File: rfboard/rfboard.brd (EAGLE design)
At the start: 30 x 60 mm, 30 parts, among them Q1 IRLML5203, Q2 IRLML5203, Q3 IRLML5203, Q4 IRLML5203, Q5 IRLML5203

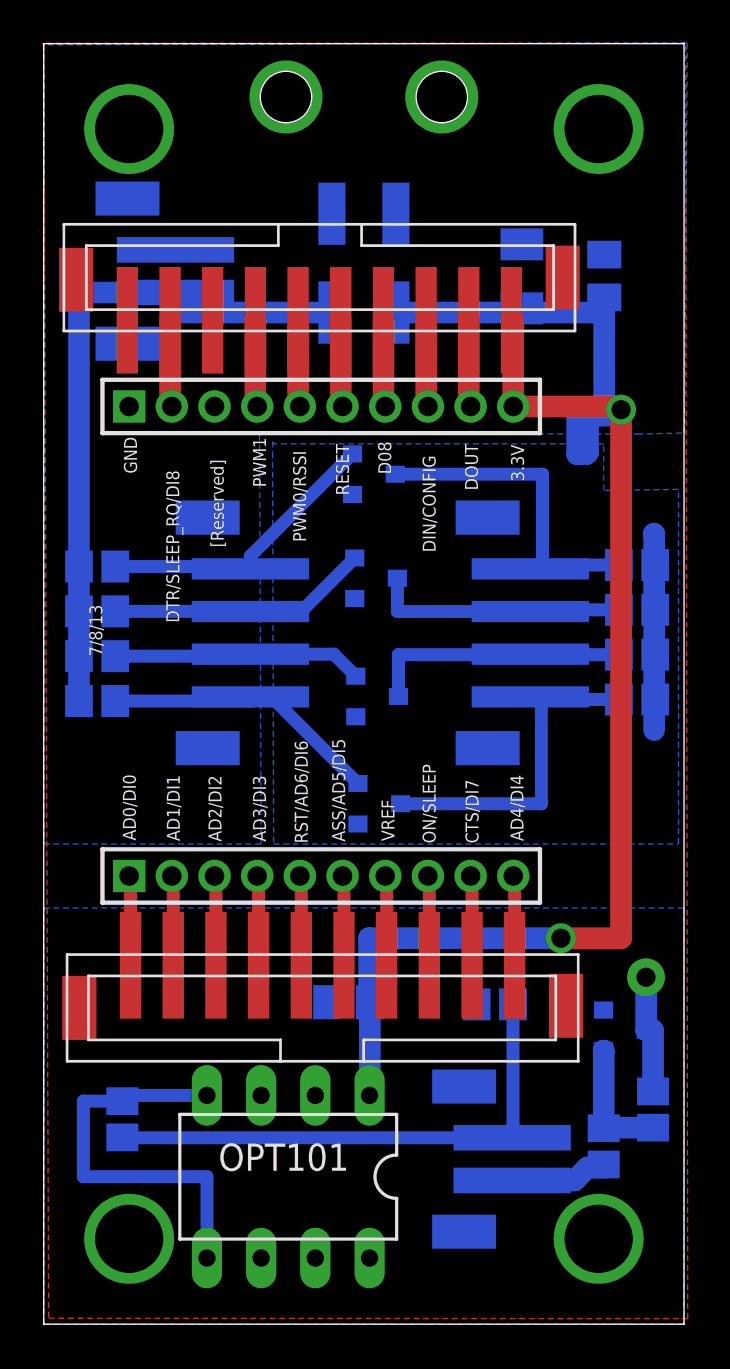
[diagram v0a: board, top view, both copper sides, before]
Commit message: resolved Sparkfun DRC errors, except for in-between pin errors
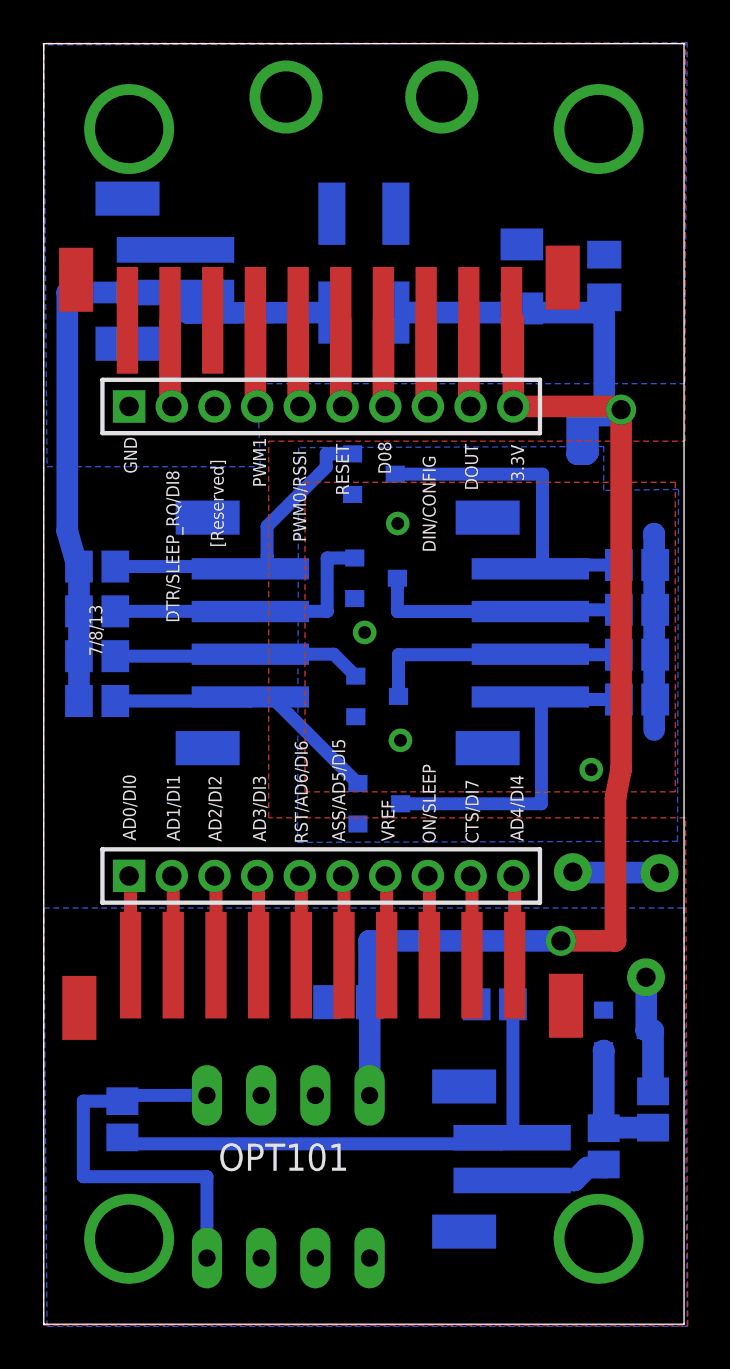
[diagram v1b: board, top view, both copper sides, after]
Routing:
- net GND: track 5.68 -> 9.69 mm, vias 1 -> 3
- net H2: track 12.3 -> 13.7 mm
- net H1: track 13.8 -> 15.0 mm
- net AMB_LOW: track 24.5 -> 25.1 mm
- net 3.3V: track 84.0 -> 83.8 mm, vias 2 -> 6
- added copper zone on layer 1, net 3.3V

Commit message: hole size, wire distance fixes, no soldermask changes yet
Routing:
- net GND: track 9.69 -> 72.3 mm, vias 3 -> 5
- net 3.3V: track 83.8 -> 84.6 mm
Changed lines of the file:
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@@
 <contactref element="C18" pad="2"/>
 <contactref element="C19" pad="2"/>
-<polygon width="0.508" layer="16" isolate="0.254">
+<polygon width="0.508" layer="16" isolate="0.3048">
 <vertex x="0.1524" y="40.1784"/>
-<vertex x="10.1524" y="40.1784"/>
-<vertex x="10" y="44.069"/>
-<vertex x="30.0228" y="44.069"/>
+<vertex x="5.2248" y="40.2038"/>
+<vertex x="5.1486" y="46.736"/>
+<vertex x="29.972" y="46.6852"/>
 <vertex x="30.1498" y="60.0456"/>
 <vertex x="0" y="59.944"/>
@@
 <via x="28.8544" y="21.1328" extent="1-16" drill="0.9" diameter="1.778"/>
 <via x="24.7904" y="21.1836" extent="1-16" drill="0.9" diameter="1.778"/>
-<wire x1="24.7904" y1="21.1582" x2="28.8036" y2="21.1582" width="1.016" layer="16"/>
-<wire x1="24.7904" y1="21.1836" x2="24.7904" y2="21.1582" width="0" layer="19" extent="16-16"/>
-<wire x1="28.8544" y1="21.1328" x2="28.8036" y2="21.1582" width="0" layer="19" extent="16-16"/>
-<wire x1="6.1724" y1="50.3394" x2="3.917" y2="47.0366" width="0" layer="19" extent="1-16"/>
+<wire x1="24.7904" y1="21.1582" x2="28.448" y2="21.1582" width="1.016" layer="16"/>
+<wire x1="28.448" y1="21.1582" x2="28.8036" y2="21.1582" width="1.016" layer="16"/>
+<wire x1="28.448" y1="21.336" x2="28.448" y2="21.1582" width="0.508" layer="16"/>
+<wire x1="28.448" y1="21.336" x2="28.8544" y2="21.1328" width="0.508" layer="16"/>
+<wire x1="22.86" y1="22.86" x2="24.384" y2="21.336" width="0.508" layer="16"/>
+<wire x1="16.256" y1="22.86" x2="22.86" y2="22.86" width="0.508" layer="16"/>
+<wire x1="3.048" y1="22.86" x2="16.256" y2="22.86" width="0.508" layer="1"/>
+<wire x1="3.048" y1="45.212" x2="3.048" y2="22.86" width="0.508" layer="1"/>
+<wire x1="4.572" y1="46.736" x2="3.048" y2="45.212" width="0.508" layer="1"/>
+<wire x1="4.572" y1="49.784" x2="4.572" y2="46.736" width="0.508" layer="1"/>
+<wire x1="9.144" y1="54.356" x2="4.572" y2="49.784" width="0.508" layer="1"/>
+<wire x1="14.732" y1="54.356" x2="9.144" y2="54.356" width="0.508" layer="1"/>
+<wire x1="24.384" y1="21.336" x2="24.7904" y2="21.1836" width="0.508" layer="16"/>
+<via x="16.256" y="22.86" extent="1-16" drill="0.508"/>
+<via x="14.732" y="54.356" extent="1-16" drill="0.508"/>
+<wire x1="24.7904" y1="21.1582" x2="24.7904" y2="21.1836" width="0" layer="19" extent="16-16"/>
 </signal>
 <signal name="AMB_OUT">
@@
 <contactref element="U$3" pad="P$1"/>
 <contactref element="X1" pad="P$3"/>
-<wire x1="16.5" y1="47.4" x2="26.2612" y2="47.4" width="1.016" layer="16"/>
+<wire x1="16.5" y1="47.4" x2="22.86" y2="47.4" width="1.016" layer="16"/>
+<wire x1="22.86" y1="47.4" x2="26.2612" y2="47.4" width="1.016" layer="16"/>
 <wire x1="26.2612" y1="47.4" x2="26.2612" y2="48.1146" width="1.016" layer="16"/>
 <via x="24.2316" y="17.9578" extent="1-16" drill="0.9"/>
@@
 <via x="16.5862" y="37.5158" extent="1-16" drill="0.6"/>
 <via x="15.0368" y="32.4104" extent="1-16" drill="0.6"/>
-<wire x1="22" y1="47.0366" x2="22.4036" y2="47.5946" width="0" layer="19" extent="1-16"/>
+<wire x1="22.86" y1="47.752" x2="22.4036" y2="47.5946" width="0.508" layer="16"/>
+<wire x1="22.86" y1="47.752" x2="22.86" y2="47.4" width="0.508" layer="16"/>
+<wire x1="14.7226" y1="23.434" x2="16.7132" y2="27.3558" width="0" layer="19" extent="16-16"/>
 </signal>
 <signal name="5V" class="1">
@@
 <signal name="DTR/SLEEP_RQ/D18">
 <contactref element="U$3" pad="P$9"/>
-<wire x1="5.917" y1="43" x2="5.917" y2="47.0366" width="1.016" layer="1"/>
+<wire x1="5.917" y1="43" x2="5.917" y2="43.18" width="1.016" layer="1"/>
 <contactref element="JP1" pad="2"/>
-<wire x1="6" y1="43" x2="5.917" y2="43" width="0" layer="19" extent="1-1"/>
+<wire x1="5.917" y1="43.18" x2="5.917" y2="47.0366" width="1.016" layer="1"/>
+<wire x1="6.096" y1="43.18" x2="6" y2="43" width="0.254" layer="1"/>
+<wire x1="6.096" y1="43.18" x2="5.917" y2="43.18" width="0.254" layer="1"/>
 </signal>
 <signal name="PWM1">
@@
 <contactref element="R8" pad="2"/>
 <wire x1="16.7226" y1="24.384" x2="23.3172" y2="24.384" width="0.6096" layer="16"/>
-<wire x1="23.3172" y1="24.384" x2="23.3172" y2="29.21" width="0.6096" layer="16"/>
+<wire x1="23.3172" y1="24.384" x2="23.3172" y2="29.2698" width="0.6096" layer="16"/>
 <wire x1="23.3172" y1="29.2698" x2="23.3172" y2="29.4132" width="0.6096" layer="16"/>
 <wire x1="23.3172" y1="29.4132" x2="22.8" y2="29.4132" width="0.6096" layer="16"/>
 <wire x1="22.8" y1="29.4132" x2="22.8" y2="29.391" width="0.6096" layer="16"/>
 <wire x1="26.95" y1="29.2698" x2="23.3172" y2="29.2698" width="0.6096" layer="16"/>
-<wire x1="23.3172" y1="29.2698" x2="23.3172" y2="29.21" width="0.6096" layer="16"/>
 </signal>
 <signal name="L3">
